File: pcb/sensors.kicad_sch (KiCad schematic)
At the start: 5 parts, among them U3 INA230AIRGTT, U4 MCP9804_DFN, U6 INA230AIRGTT

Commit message: hierarchy and power sequencing, level shift
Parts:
- U3: symbol library:INA230AIRGTT_1 -> library:INA230AIRGTT_1_1
- U6: symbol library:INA230AIRGTT_2 -> library:INA230AIRGTT_2_1
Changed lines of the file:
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@@
 	)
 	(symbol
-		(lib_name "INA230AIRGTT_1_1")
-		(lib_id "library:INA230AIRGTT_1")
+		(lib_name "INA230AIRGTT_1_1_1")
+		(lib_id "library:INA230AIRGTT_1_1")
 		(at 133.35 76.2 0)
 		(unit 1)
@@
 	)
 	(symbol
-		(lib_name "INA230AIRGTT_2_1")
-		(lib_id "library:INA230AIRGTT_2")
+		(lib_name "INA230AIRGTT_2_1_1")
+		(lib_id "library:INA230AIRGTT_2_1")
 		(at 133.35 119.38 0)
 		(unit 1)

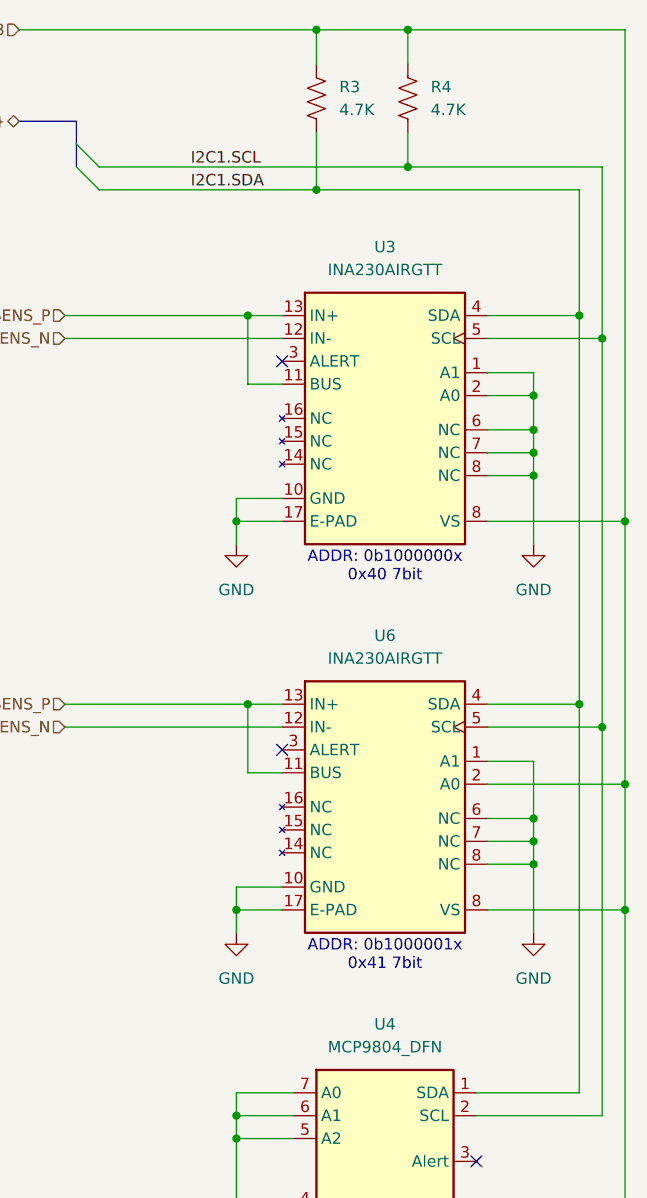
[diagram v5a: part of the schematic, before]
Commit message: defined memory pinouts
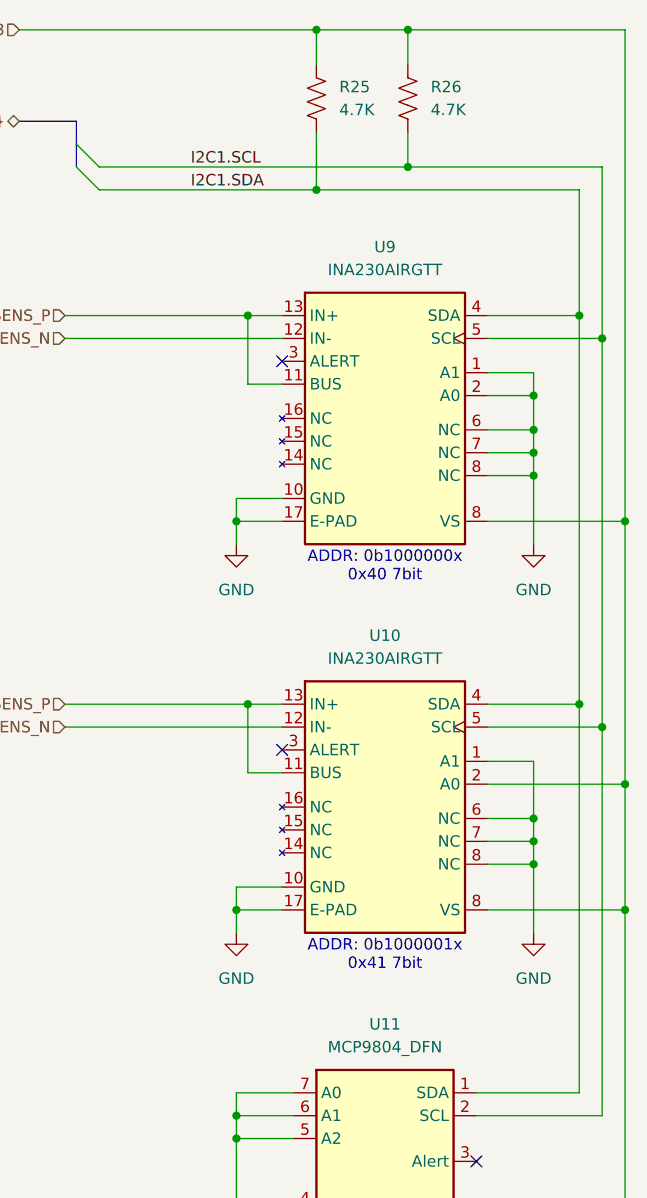
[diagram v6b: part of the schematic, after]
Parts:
- renumbered R3 to R25, R4 to R26, U6 to U10, U4 to U11, U3 to U9
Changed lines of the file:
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@@
 		(dnp no)
 		(fields_autoplaced yes)
-		(property "Reference" "#PWR015"
+		(property "Reference" "#PWR030"
 			(at 149.86 139.7 0)
 			(effects
@@
 			(project "RPi-HwAB-1"
 				(path "/e63e39d7-6ac0-4ffd-8aa3-1841a4541b55/010325a2-ae86-4ae0-96e8-1d16e8e45471"
-					(reference "#PWR015")
+					(reference "#PWR030")
 					(unit 1)
 				)
@@
 		(on_board yes)
 		(dnp no)
-		(property "Reference" "R3"
+		(property "Reference" "R25"
 			(at 128.27 39.37 0)
 			(effects
@@
 			(project "RPi-HwAB-1"
 				(path "/e63e39d7-6ac0-4ffd-8aa3-1841a4541b55/010325a2-ae86-4ae0-96e8-1d16e8e45471"
-					(reference "R3")
+					(reference "R25")
 					(unit 1)
 				)
@@
 		(on_board yes)
 		(dnp no)
-		(property "Reference" "U4"
+		(property "Reference" "U11"
 			(at 133.35 143.51 0)
 			(effects
@@
 			(project ""
 				(path "/e63e39d7-6ac0-4ffd-8aa3-1841a4541b55/010325a2-ae86-4ae0-96e8-1d16e8e45471"
-					(reference "U4")
+					(reference "U11")
 					(unit 1)
 				)
@@
 		(dnp no)
 		(fields_autoplaced yes)
-		(property "Reference" "#PWR04"
+		(property "Reference" "#PWR029"
 			(at 149.86 96.52 0)
 			(effects
@@
 			(project "RPi-HwAB-1"
 				(path "/e63e39d7-6ac0-4ffd-8aa3-1841a4541b55/010325a2-ae86-4ae0-96e8-1d16e8e45471"
-					(reference "#PWR04")
+					(reference "#PWR029")
 					(unit 1)
 				)
@@
 		(dnp no)
 		(fields_autoplaced yes)
-		(property "Reference" "#PWR014"
+		(property "Reference" "#PWR028"
 			(at 116.84 176.53 0)
 			(effects
@@
 			(project "RPi-HwAB-1"
 				(path "/e63e39d7-6ac0-4ffd-8aa3-1841a4541b55/010325a2-ae86-4ae0-96e8-1d16e8e45471"
-					(reference "#PWR014")
+					(reference "#PWR028")
 					(unit 1)
 				)
@@
 		(dnp no)
 		(fields_autoplaced yes)
-		(property "Reference" "#PWR01"
+		(property "Reference" "#PWR026"
 			(at 116.84 96.52 0)
 			(effects
@@
 			(project ""
 				(path "/e63e39d7-6ac0-4ffd-8aa3-1841a4541b55/010325a2-ae86-4ae0-96e8-1d16e8e45471"
-					(reference "#PWR01")
+					(reference "#PWR026")
 					(unit 1)
 				)
@@
 		(dnp no)
 		(fields_autoplaced yes)
-		(property "Reference" "U3"
+		(property "Reference" "U9"
 			(at 133.35 57.15 0)
 			(effects
@@
 			(project ""
 				(path "/e63e39d7-6ac0-4ffd-8aa3-1841a4541b55/010325a2-ae86-4ae0-96e8-1d16e8e45471"
-					(reference "U3")
+					(reference "U9")
 					(unit 1)
 				)
@@
 		(dnp no)
 		(fields_autoplaced yes)
-		(property "Reference" "#PWR012"
+		(property "Reference" "#PWR027"
 			(at 116.84 139.7 0)
 			(effects
@@
 			(project "RPi-HwAB-1"
 				(path "/e63e39d7-6ac0-4ffd-8aa3-1841a4541b55/010325a2-ae86-4ae0-96e8-1d16e8e45471"
-					(reference "#PWR012")
+					(reference "#PWR027")
 					(unit 1)
 				)
@@
 		(dnp no)
 		(fields_autoplaced yes)
-		(property "Reference" "R4"
+		(property "Reference" "R26"
 			(at 138.43 39.3699 0)
 			(effects
@@
 			(project ""
 				(path "/e63e39d7-6ac0-4ffd-8aa3-1841a4541b55/010325a2-ae86-4ae0-96e8-1d16e8e45471"
-					(reference "R4")
+					(reference "R26")
 					(unit 1)
 				)
@@
 		(dnp no)
 		(fields_autoplaced yes)
-		(property "Reference" "U6"
+		(property "Reference" "U10"
 			(at 133.35 100.33 0)
 			(effects
@@
 			(project "RPi-HwAB-1"
 				(path "/e63e39d7-6ac0-4ffd-8aa3-1841a4541b55/010325a2-ae86-4ae0-96e8-1d16e8e45471"
-					(reference "U6")
-					(unit 1)
-				)
+					(reference "U10")
+					(unit 1)
+				)

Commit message: power restructuring
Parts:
- U10: symbol library:INA230AIRGTT_2_1 -> library:INA230AIRGTT_1
- U9: symbol library:INA230AIRGTT_1_1 -> library:INA230AIRGTT
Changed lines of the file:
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@@
 	)
 	(symbol
-		(lib_name "INA230AIRGTT_1_1_1")
-		(lib_id "library:INA230AIRGTT_1_1")
+		(lib_name "INA230AIRGTT_2")
+		(lib_id "library:INA230AIRGTT")
 		(at 133.35 76.2 0)
 		(unit 1)
@@
 		)
 		(property "Description" "36-V, 16-bit, I²C output current, voltage and power monitor with alert"
+			(at 133.35 76.2 0)
+			(effects
+				(font
+					(size 1.27 1.27)
+				)
+				(hide yes)
+			)
+		)
+		(property "Name" ""
 			(at 133.35 76.2 0)
 			(effects
@@
 	)
 	(symbol
-		(lib_name "INA230AIRGTT_2_1_1")
-		(lib_id "library:INA230AIRGTT_2_1")
+		(lib_name "INA230AIRGTT_1_1")
+		(lib_id "library:INA230AIRGTT_1")
 		(at 133.35 119.38 0)
 		(unit 1)
@@
 			(at 133.35 119.38 0)
 			(effects
+				(font
+					(size 1.27 1.27)
+				)
+				(hide yes)
+			)
+		)
+		(property "Name" ""
+			(at 133.35 119.38 0)
+			(effects

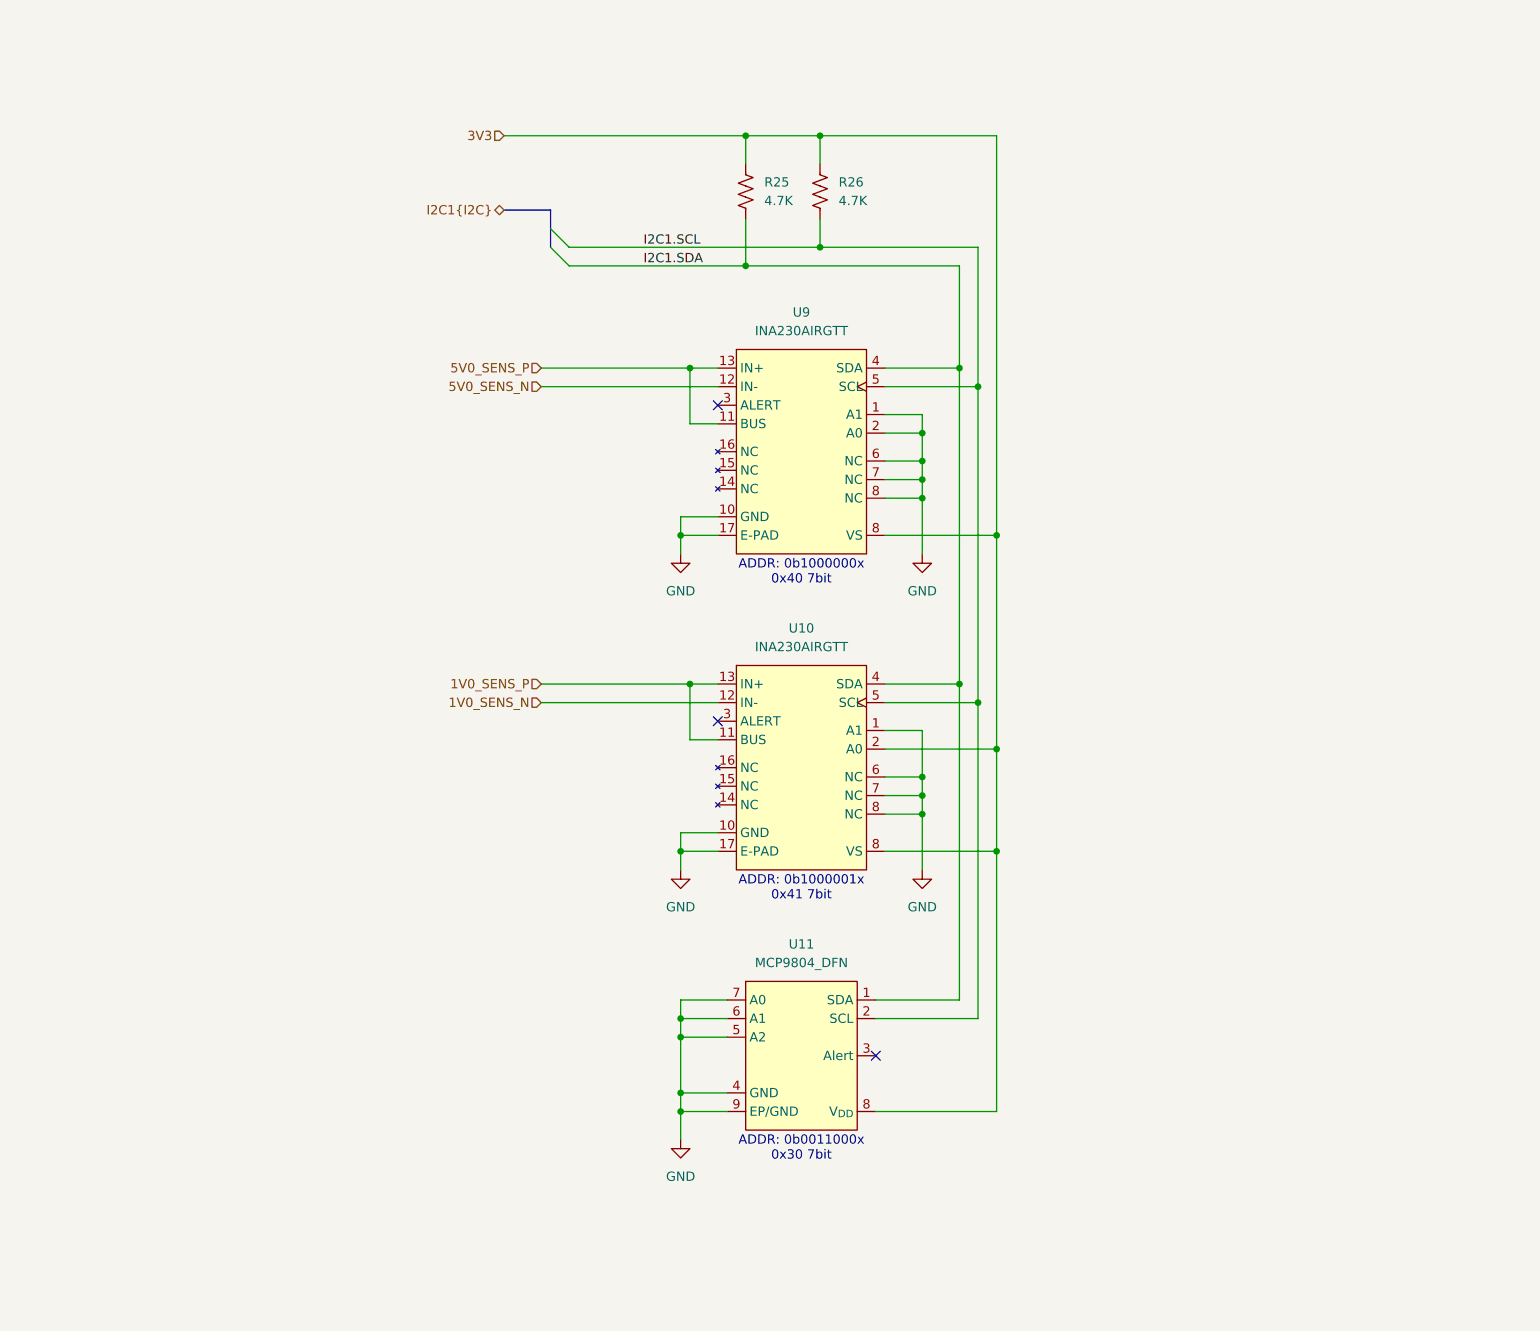
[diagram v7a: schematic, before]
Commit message: changes to power tree
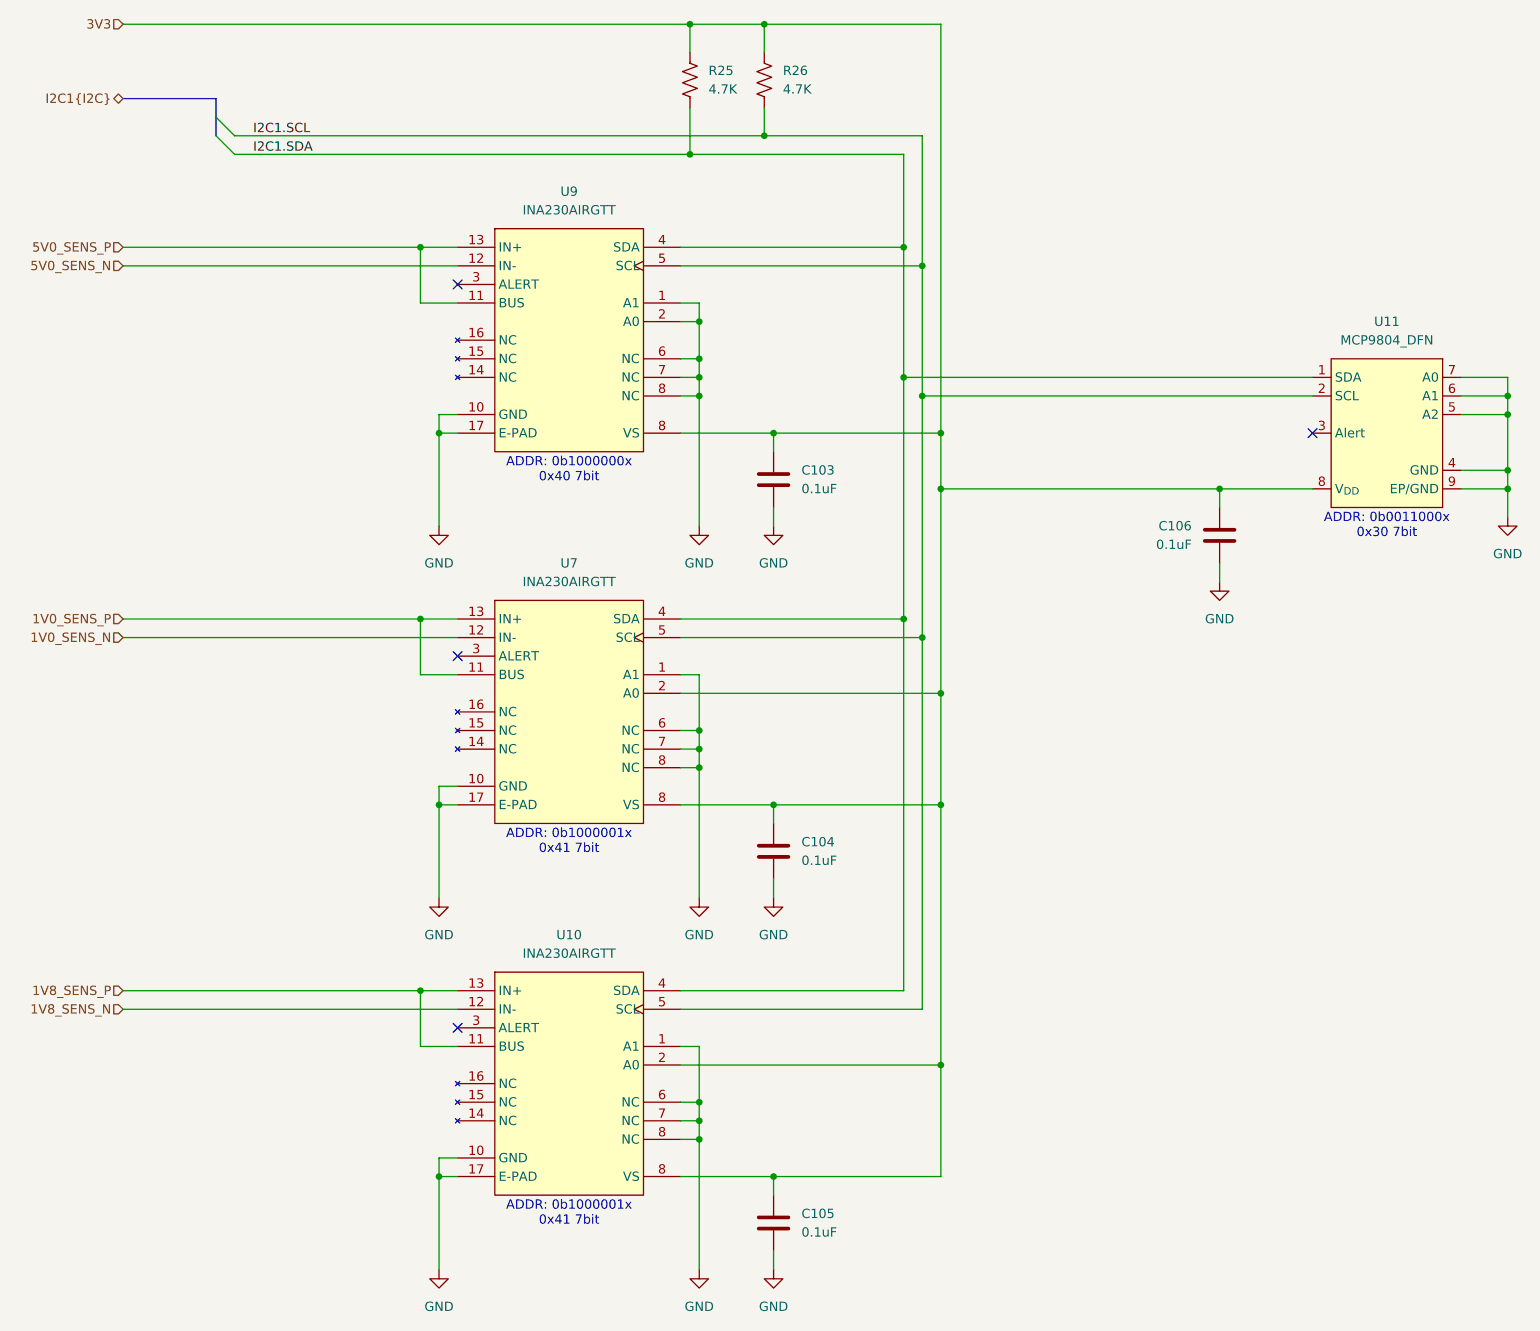
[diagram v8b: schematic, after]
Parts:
- removed U10: INA230AIRGTT, Package_DFN_QFN:VQFN-16-1EP_3x3mm_P0.5mm_EP1.6x1.6mm, symbol library:INA230AIRGTT_1
- added C103, C104, C105, C106: 0.1uF, Capacitor_SMD:C_0402_1005Metric, symbol Device:C
- added U10, U7: INA230AIRGTT, Package_DFN_QFN:VQFN-16-1EP_3x3mm_P0.5mm_EP1.6x1.6mm, symbol library:INA230AIRGTT
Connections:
- net 1V0_SENS_N: now also U7.12 (IN-)
- net 1V0_SENS_P: now also U7.11 (BUS), U7.13 (IN+)
- net 3V3: now also C103.1, C104.1, C105.1, C106.1, U10.2 (A0), U10.8 (VS), U7.2 (A0), U7.8 (VS)
- net GND: now also C103.2, C104.2, C105.2, C106.2, U10.1 (A1), U10.10 (GND), U10.17 (E-PAD), U10.6 (NC), U10.7 (NC), U10.8 (VS), U7.1 (A1), U7.10 (GND), U7.17 (E-PAD), U7.6 (NC), U7.7 (NC), U7.8 (VS)
- net I2C1.SCL: now also U10.5 (SCL), U7.5 (SCL)
- net I2C1.SDA: now also U10.4 (SDA), U7.4 (SDA)
- new net 1V8_SENS_N: U10.12 (IN-)
- new net 1V8_SENS_P: U10.11 (BUS), U10.13 (IN+)
- no-connect marks 3 -> 4
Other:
- moved on the sheet: R25, R26, U11
